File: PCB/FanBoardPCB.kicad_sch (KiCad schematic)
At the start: 0 parts

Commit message: add basic symbols
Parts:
- added J1, J2, J3, J4: FAN1, symbol Connector_Generic:Conn_01x02
- added J13: FanBrdConn, symbol Connector_Generic:Conn_02x03_Top_Bottom
- added Q1, Q2: IRLML0030, Package_TO_SOT_SMD:SOT-23, symbol Transistor_FET:IRLML0030
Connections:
- new net +12V: J13.1 (Pin_1)
- new net FAN1: J13.2 (Pin_2)
- new net FAN2: J13.3 (Pin_3)
- new net FAN3: J13.5 (Pin_5)
- new net FAN4: J13.6 (Pin_6)
- new net GNDPWR: J13.4 (Pin_4)

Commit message: add initial schematic
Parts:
- added C1, C2: 100uF, symbol Device:C
- added D1, D2, D3, D4: D, symbol Device:D
- added Q3, Q4: IRLML0030, Package_TO_SOT_SMD:SOT-23, symbol Transistor_FET:IRLML0030
- added R1, R2, R3, R4, R5, R6, R7, R8: 100k, symbol Device:R
- J1: value FAN1 -> FAN3
- J2: value FAN1 -> FAN4
- J4: value FAN1 -> FAN2
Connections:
- net +12V: now also J1.1 (Pin_1), J2.1 (Pin_1), J3.1 (Pin_1), J4.1 (Pin_1), C1.1, C2.1, D1.1 (K), D2.1 (K), D3.1 (K), D4.1 (K)
- net FAN1: now also R7.2
- net FAN2: now also R8.1
- net FAN3: now also R5.1
- net FAN4: now also R6.1
- net GNDPWR: now also C1.2, C2.2
- net at Q2.1 (G): now also R4.1, R6.2
- net GND: now reaches Q2.2 (S)
- net GND: now also Q1.2 (S), Q3.2 (S), Q4.2 (S), R1.2, R2.2, R3.2, R4.2
- net at Q2.3 (D): now also J2.2 (Pin_2), D1.2 (A)
- net at J3.2 (Pin_2): now also D3.2 (A), Q4.3 (D)
- net at Q1.1 (G): now also R3.1, R5.2
- net at Q1.3 (D): now also J1.2 (Pin_2), D2.2 (A)
- net at J4.2 (Pin_2): now also D4.2 (A), Q3.3 (D)
- new net: Q3.1 (G), R1.1, R8.2
- new net: Q4.1 (G), R2.1, R7.1
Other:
- company: (none) -> LHR Solar
- title: (none) -> FanBoardPCB
- moved on the sheet: J1, J13, J2, Q1, Q2

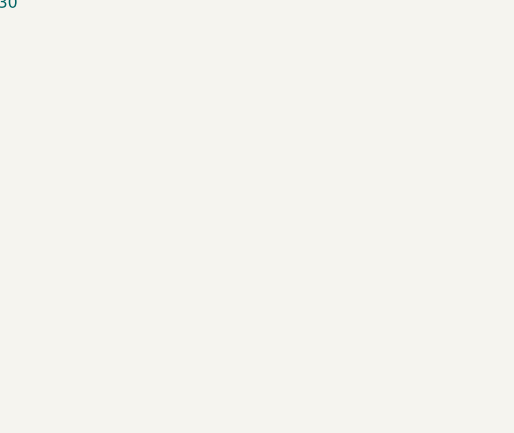
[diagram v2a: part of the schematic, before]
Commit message: add mounting holes
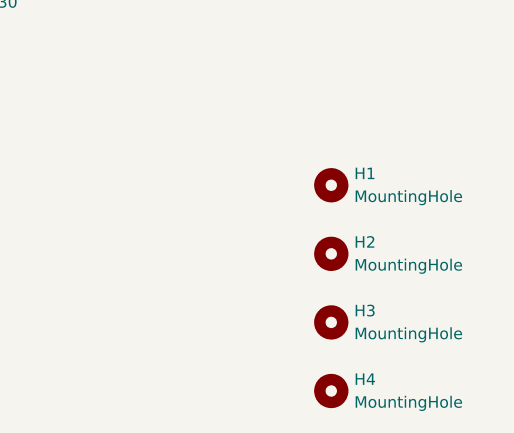
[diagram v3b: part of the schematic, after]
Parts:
- added H1, H2, H3, H4: MountingHole, symbol Mechanical:MountingHole

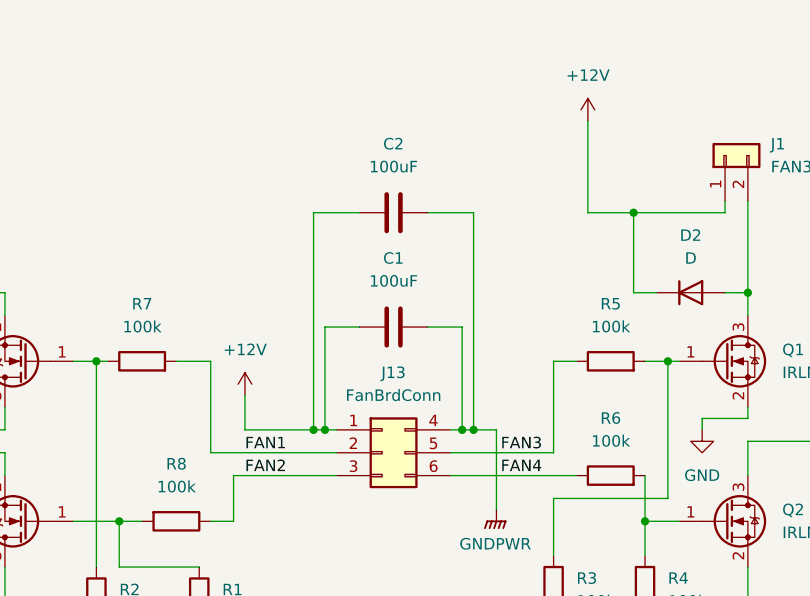
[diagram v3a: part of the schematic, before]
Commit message: add status LED and footprints
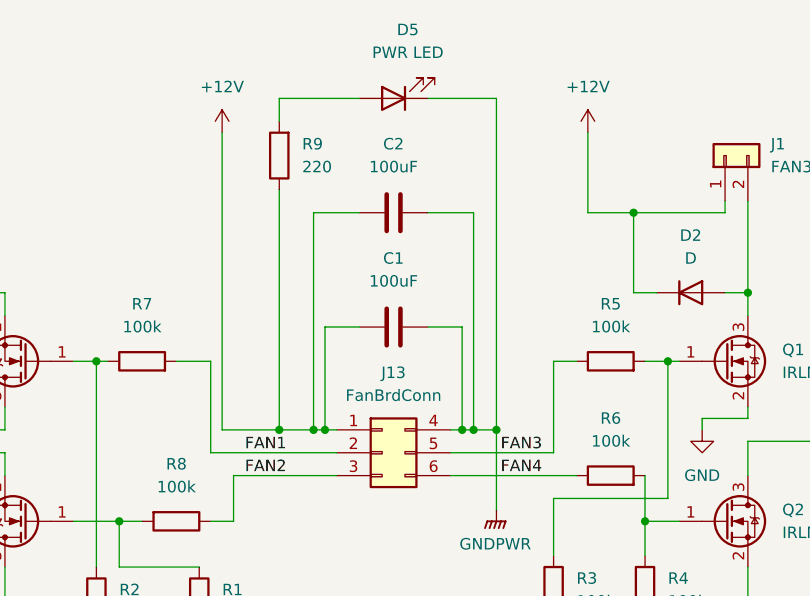
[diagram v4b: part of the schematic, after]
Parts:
- added D5: PWR LED, LED_SMD:LED_0805_2012Metric, symbol Device:LED
- added R9: 220, Resistor_SMD:R_0805_2012Metric, symbol Device:R
- C1, C2: footprint (none) -> Capacitor_SMD:C_0805_2012Metric
- D1, D2, D3, D4: footprint (none) -> Diode_SMD:D_0805_2012Metric
- H1, H2, H3, H4: footprint (none) -> MountingHole:MountingHole_3mm
- J1, J2, J3, J4: footprint (none) -> UTSVT_Connectors:Molex_MicroFit3.0_1x2xP3.00mm_PolarizingPeg_Vertical
- J13: footprint (none) -> Connector_Molex:Molex_Micro-Fit_3.0_43045-0612_2x03_P3.00mm_Vertical
- R1, R2, R3, R4, R5, R6, R7, R8: footprint (none) -> Resistor_SMD:R_0805_2012Metric
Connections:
- net +12V: now also R9.1
- net GNDPWR: now also D5.1 (K)
- new net: D5.2 (A), R9.2

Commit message: create initial layout
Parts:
- added NT1: NetTie_2, NetTie:NetTie-2_SMD_Pad2.0mm, symbol Device:NetTie_2
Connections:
- net GND: now also NT1.2
- net GNDPWR: now also NT1.1
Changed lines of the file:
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@@
 	)
 	(junction
-		(at 157.48 80.01)
+		(at 138.43 95.25)
 		(diameter 0)
 		(color 0 0 0 0)
 	)
 	(junction
-		(at 140.97 69.85)
+		(at 157.48 80.01)
 		(diameter 0)
 		(color 0 0 0 0)
@@
 	(wire
 		(pts
-			(xy 140.97 69.85) (xy 140.97 78.74)
+			(xy 138.43 69.85) (xy 138.43 95.25)
 		)
 		(stroke
@@
 	(wire
 		(pts
-			(xy 138.43 69.85) (xy 140.97 69.85)
-		)
-		(stroke
-			(width 0)
-			(type default)
-		)
-	)
-	(wire
-		(pts
 			(xy 60.96 45.72) (xy 60.96 57.15)
 		)
@@
 	(wire
 		(pts
+			(xy 138.43 69.85) (xy 140.97 69.85)
+		)
+		(stroke
+			(width 0)
+			(type default)
+		)
+	)
+	(wire
+		(pts
 			(xy 147.32 77.47) (xy 160.02 77.47)
 		)
@@
 	(wire
 		(pts
+			(xy 138.43 95.25) (xy 138.43 96.52)
+		)
+		(stroke
+			(width 0)
+			(type default)
+		)
+	)
+	(wire
+		(pts
 			(xy 121.92 69.85) (xy 123.19 69.85)
 		)
@@
 	(wire
 		(pts
+			(xy 128.27 95.25) (xy 133.35 95.25)
+		)
+		(stroke
+			(width 0)
+			(type default)
+		)
+	)
+	(wire
+		(pts
 			(xy 48.26 46.99) (xy 58.42 46.99)
 		)
@@
 	(wire
 		(pts
+			(xy 128.27 96.52) (xy 128.27 95.25)
+		)
+		(stroke
+			(width 0)
+			(type default)
+		)
+	)
+	(wire
+		(pts
 			(xy 135.89 69.85) (xy 137.16 69.85)
 		)
@@
 	)
 	(symbol
+		(lib_id "power:GND")
+		(at 128.27 96.52 0)
+		(unit 1)
+		(exclude_from_sim no)
+		(in_bom yes)
+		(on_board yes)
+		(dnp no)
+		(fields_autoplaced yes)
+		(property "Reference" "#PWR015"
+			(at 128.27 102.87 0)
+			(effects
+				(font
+					(size 1.27 1.27)
+				)
+				(hide yes)
+			)
+		)
+		(property "Value" "GND"
+			(at 128.27 101.6 0)
+			(effects
+				(font
+					(size 1.27 1.27)
+				)
+			)
+		)
+		(property "Footprint" ""
+			(at 128.27 96.52 0)
+			(effects
+				(font
+					(size 1.27 1.27)
+				)
+				(hide yes)
+			)
+		)
+		(property "Datasheet" ""
+			(at 128.27 96.52 0)
+			(effects
+				(font
+					(size 1.27 1.27)
+				)
+				(hide yes)
+			)
+		)
+		(property "Description" "Power symbol creates a global label with name \"GND\" , ground"
+			(at 128.27 96.52 0)
+			(effects
+				(font
+					(size 1.27 1.27)
+				)
+				(hide yes)
+			)
+		)
+		(pin "1"
+		)
+		(instances
+			(project "FanBoardPCB"
+				(path "/1aabcb47-8889-428a-a945-776d6a97cab7"
+					(reference "#PWR015")
+					(unit 1)
+				)
+			)
+		)
+	)
+	(symbol
 		(lib_id "Mechanical:MountingHole")
 		(at 217.17 109.22 0)
@@
 	(symbol
 		(lib_id "power:GNDPWR")
-		(at 140.97 78.74 0)
+		(at 138.43 96.52 0)
 		(unit 1)
 		(exclude_from_sim no)
@@
 		(fields_autoplaced yes)
 		(property "Reference" "#PWR02"
-			(at 140.97 83.82 0)
+			(at 138.43 101.6 0)
 			(effects
 				(font
@@
 		)
 		(property "Value" "GNDPWR"
-			(at 140.843 82.55 0)
+			(at 138.303 100.33 0)
 			(effects
 				(font
@@
 		)
 		(property "Footprint" ""
-			(at 140.97 80.01 0)
+			(at 138.43 97.79 0)
 			(effects
 				(font
@@
 		)
 		(property "Datasheet" ""
-			(at 140.97 80.01 0)
+			(at 138.43 97.79 0)
 			(effects
 				(font
@@
 		)
 		(property "Description" "Power symbol creates a global label with name \"GNDPWR\" , global ground"
-			(at 140.97 78.74 0)
+			(at 138.43 96.52 0)
 			(effects
 				(font
@@
 					(unit 1)
 				)
+			)
+		)
+	)
+	(symbol
+		(lib_id "Device:NetTie_2")
+		(at 135.89 95.25 180)
+		(unit 1)
+		(exclude_from_sim no)
+		(in_bom no)
+		(on_board yes)
+		(dnp no)
+		(property "Reference" "NT1"
+			(at 135.89 90.17 0)
+			(effects
+				(font
+					(size 1.27 1.27)
+				)
+				(hide yes)
+			)
+		)
+		(property "Value" "NetTie_2"
+			(at 135.89 92.71 0)
+			(effects
+				(font
+					(size 1.27 1.27)
+				)
+				(hide yes)
+			)
+		)
+		(property "Footprint" "NetTie:NetTie-2_SMD_Pad2.0mm"
+			(at 135.89 95.25 0)
+			(effects
+				(font
+					(size 1.27 1.27)
+				)
+				(hide yes)
+			)
+		)
+		(property "Datasheet" "~"
+			(at 135.89 95.25 0)
+			(effects
+				(font
+					(size 1.27 1.27)
+				)
+				(hide yes)
+			)
+		)
+		(property "Description" "Net tie, 2 pins"
+			(at 135.89 95.25 0)
+			(effects
+				(font
+					(size 1.27 1.27)
+				)
+				(hide yes)
+			)
+		)
+		(pin "1"
+		)
+		(pin "2"
+		)
+		(instances
+			(project ""
+				(path "/1aabcb47-8889-428a-a945-776d6a97cab7"
+					(reference "NT1")
+					(unit 1)
+				)

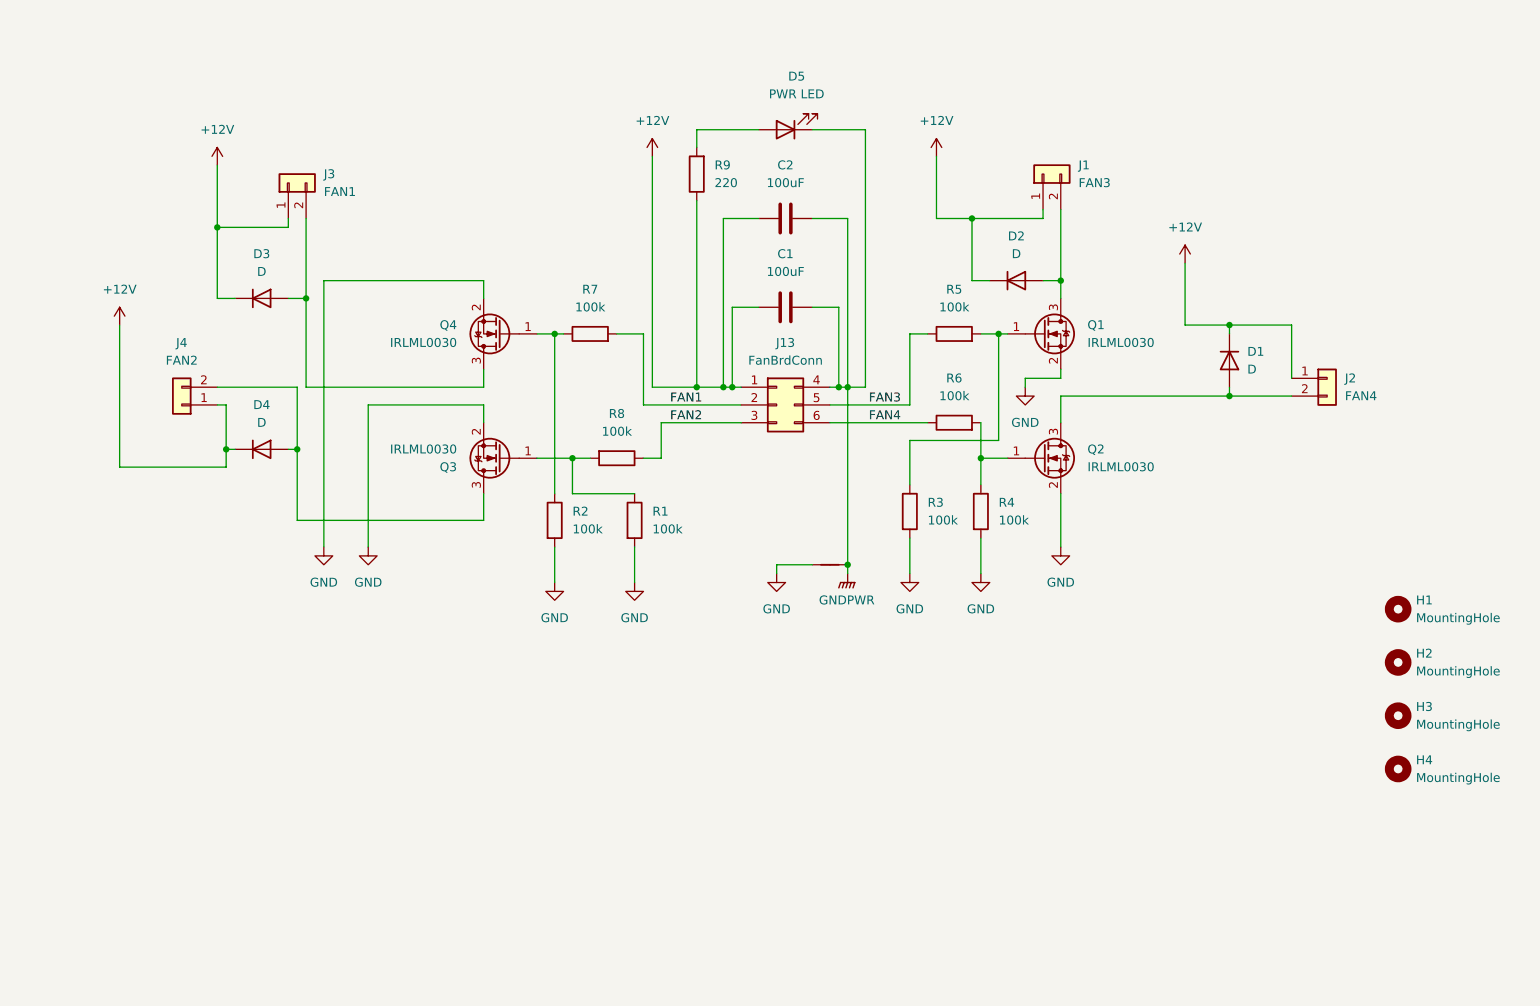
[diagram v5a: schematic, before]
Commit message: better layout and traces
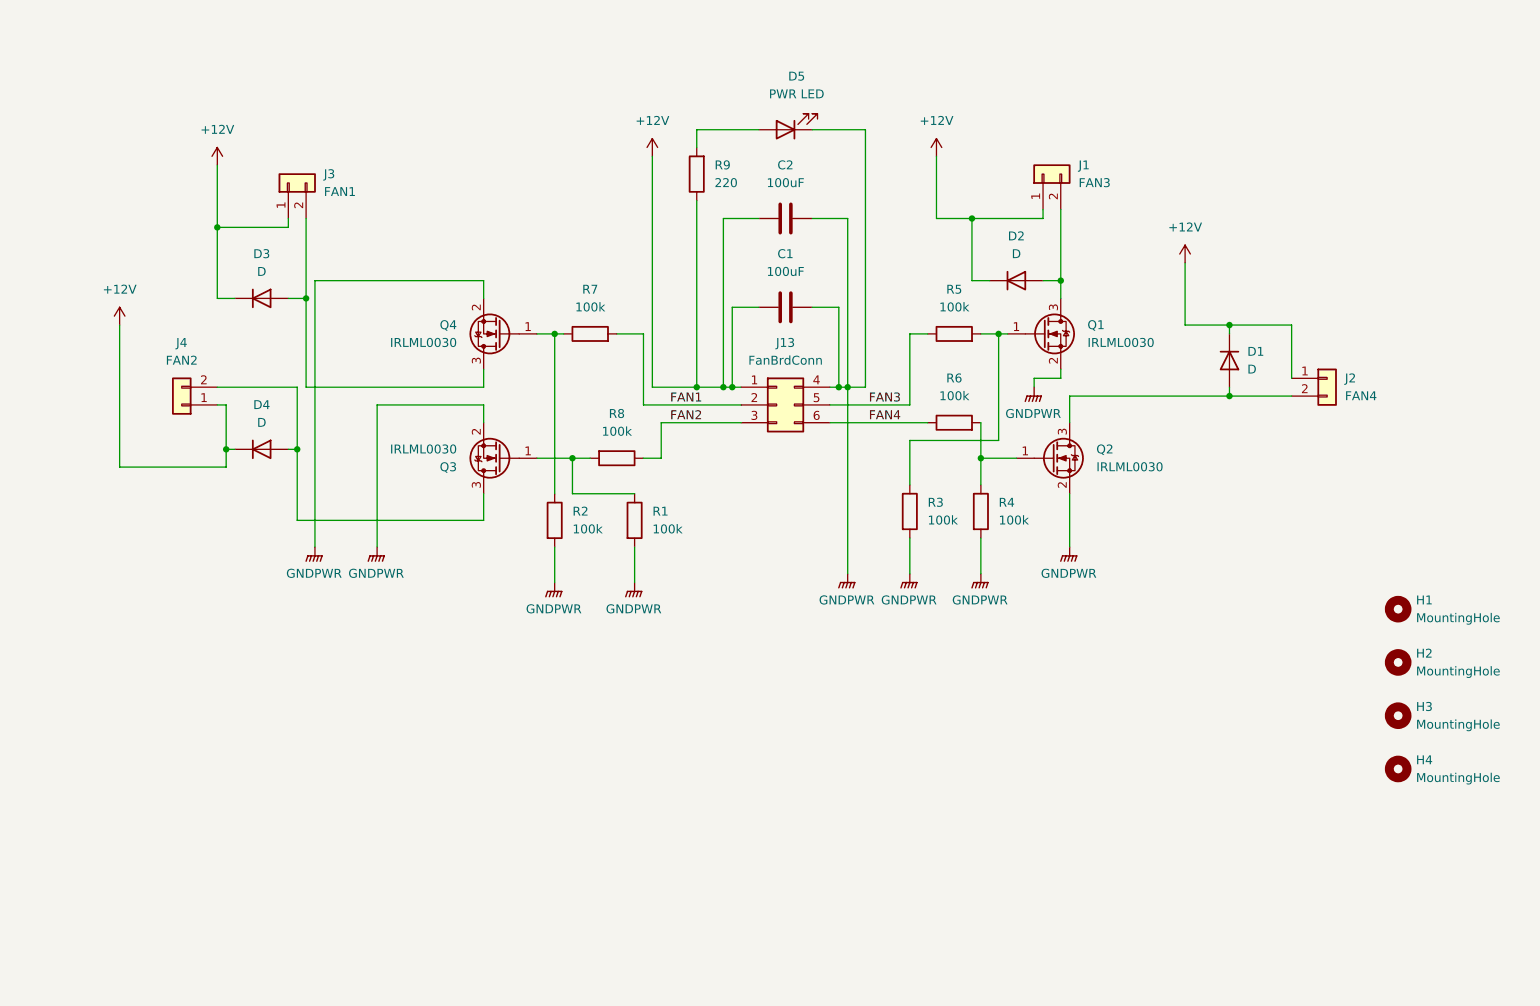
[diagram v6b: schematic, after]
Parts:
- removed NT1: NetTie_2, NetTie:NetTie-2_SMD_Pad2.0mm, symbol Device:NetTie_2
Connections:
- net GND is gone; now on net GNDPWR: Q1.2 (S), Q2.2 (S), Q3.2 (S), Q4.2 (S), R1.2, R2.2, R3.2, R4.2
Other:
- moved on the sheet: Q2

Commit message: add net labels
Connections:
- net Q3-Gate: now reaches Q3.1 (G), R1.1, R8.2
- net Q4-Drain: now reaches D3.2 (A), J3.2 (Pin_2), Q4.3 (D)
- net Q3-Drain: now reaches D4.2 (A), J4.2 (Pin_2), Q3.3 (D)
- net Q1-Drain: now reaches D2.2 (A), J1.2 (Pin_2), Q1.3 (D)
- net Q2-Gate: now reaches Q2.1 (G), R4.1, R6.2
- net Q2-Drain: now reaches D1.2 (A), J2.2 (Pin_2), Q2.3 (D)
- net LED+: now reaches D5.2 (A), R9.2
- net Q4-Gate: now reaches Q4.1 (G), R2.1, R7.1
- net Q1-Gate: now reaches Q1.1 (G), R3.1, R5.2
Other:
- moved on the sheet: D1, J2, Q1, Q2, R7

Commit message: cleanup PCB
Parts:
- J3: value FAN1 -> FAN2
- J4: value FAN2 -> FAN1
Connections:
- net Q3-Drain: now also J3.2 (Pin_2), Q4.3 (D); no longer J4.2 (Pin_2), Q3.3 (D)
- net Q3-Gate: now also Q4.1 (G); no longer Q3.1 (G)
- net Q4-Drain: now also J4.2 (Pin_2), Q3.3 (D); no longer J3.2 (Pin_2), Q4.3 (D)
- net Q4-Gate: now also Q3.1 (G); no longer Q4.1 (G)
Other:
- moved on the sheet: C1, C2, D1, D5, H1, H2, H3, H4, J1, J13, J2, Q1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
